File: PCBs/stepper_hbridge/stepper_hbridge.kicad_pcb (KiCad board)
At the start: 2 copper layers, 52.5 x 54.4 mm, 34 parts, among them J1 Conn_02x07_Odd_Even, J2 Conn_02x08_Odd_Even, J3 Conn_02x08_Odd_Even, J4 Conn_01x04_Pin, J5 Conn_01x04_Pin, J6 Conn_01x02_Pin, U1 L298N, U2 L298N, U3 NCP718xSN500

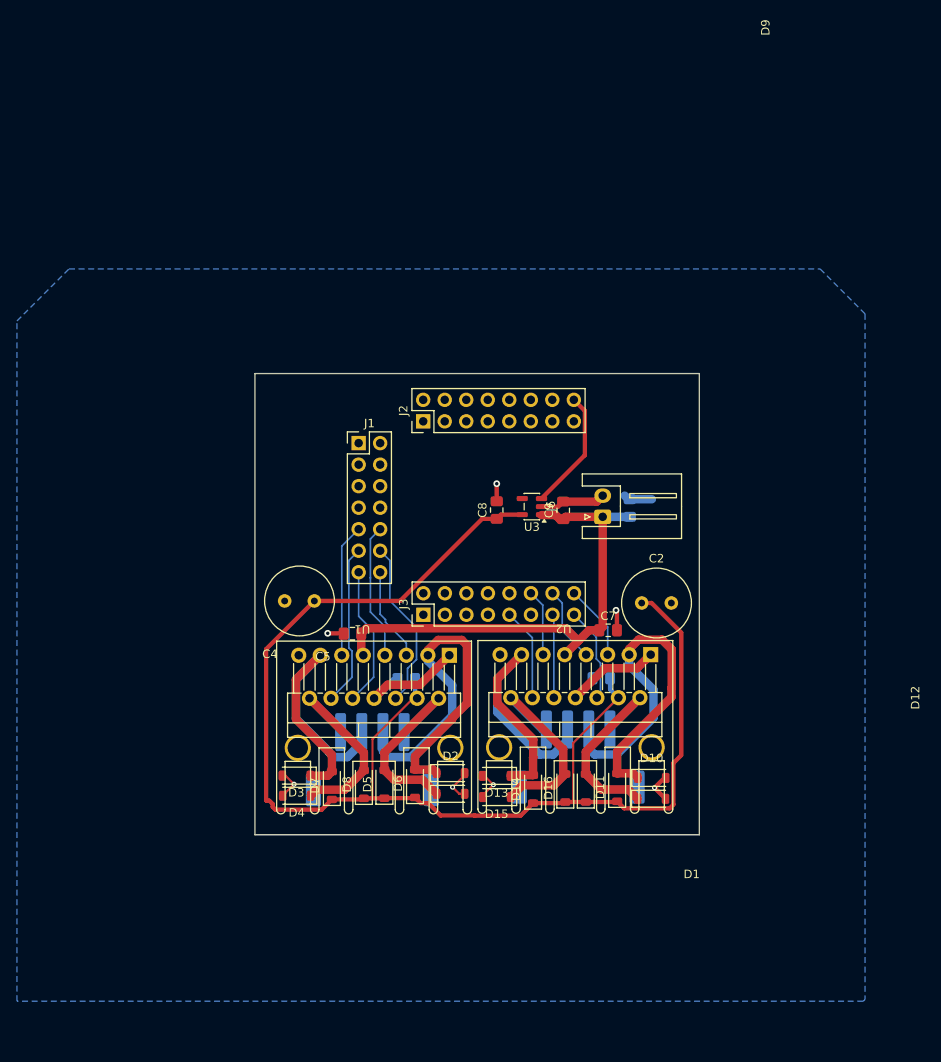
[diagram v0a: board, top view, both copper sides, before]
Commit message: fixed errors, need to add quadrature
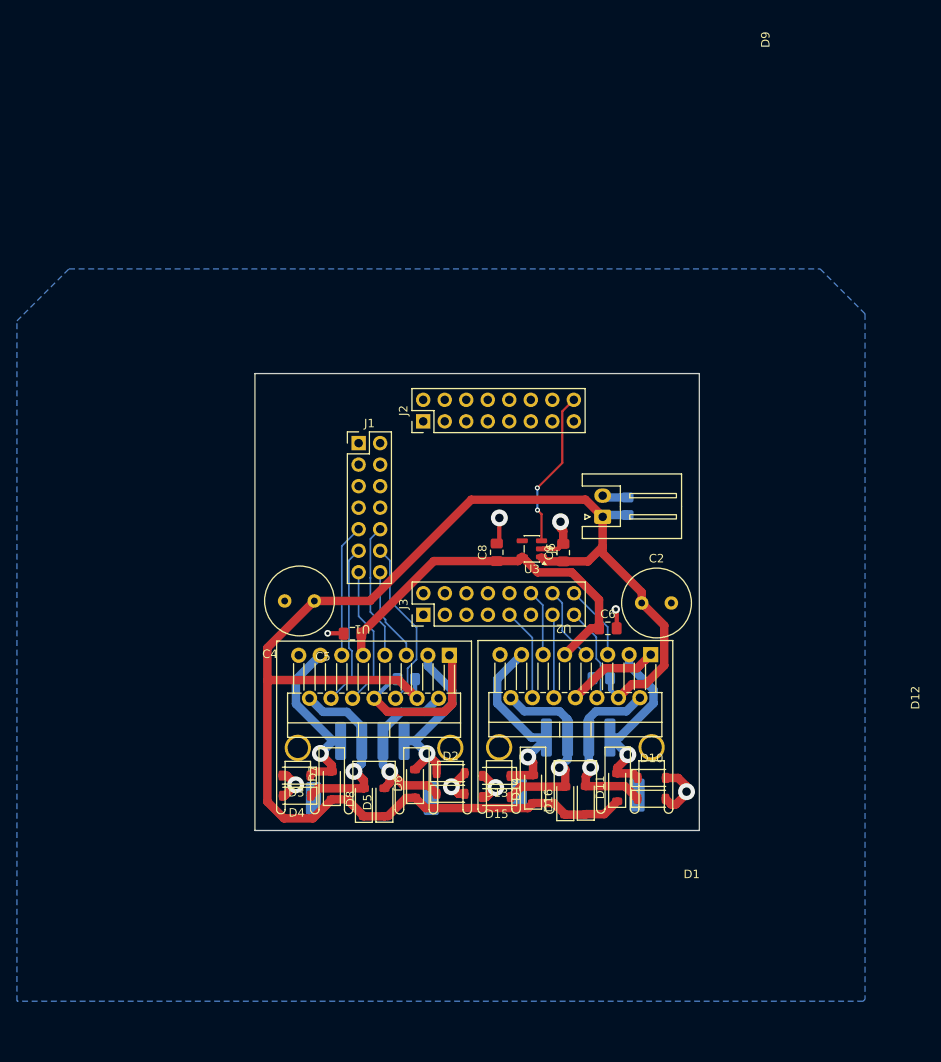
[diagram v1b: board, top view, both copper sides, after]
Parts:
- C6: moved to F.Cu
- C7: moved to B.Cu
- moved C7 14.8 mm to (158.0, 66.7), turned to 90 degrees
- moved C6 14.4 mm to (155.7, 81.1), turned to 0 degrees
- moved C8 4.99 mm to (142.6, 72.1)
- moved C9 4.99 mm to (150.4, 72.2)
- moved U3 4.99 mm to (146.7, 71.7)
- moved D5 2.12 mm to (129.3, 101.6)
- moved D8 2.12 mm to (126.9, 101.6)
- moved D16 1.49 mm to (150.7, 101.4)
- moved D9 1.43 mm to (153.1, 101.4)
- moved J4 1.04 mm to (127.9, 97.6)
- moved J5 0.95 mm to (152.2, 97.2)
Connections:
- C1 pad 1: +5V -> +24V
- C2 pad 1: +5V -> +24V
- C3 pad 1: +5V -> +24V
- C4 pad 1: +5V -> +24V
- C5 pad 1: +24V -> +5V
- C6 pad 1: +24V -> +5V
- D11 pad 1: +5V -> +24V
- D14 pad 1: +5V -> +24V
- D16 pad 1: +5V -> +24V
- D5 pad 1: +5V -> +24V
- D6 pad 1: +5V -> +24V
- D7 pad 1: +5V -> +24V
- D8 pad 1: +5V -> +24V
- D9 pad 1: +5V -> +24V
- J4 pad 1: Net-(D1-K) -> Net-(D2-K)
- J4 pad 2: Net-(D2-K) -> Net-(D1-K)
- J4 pad 3: Net-(D3-K) -> Net-(D4-K)
- J4 pad 4: Net-(D4-K) -> Net-(D3-K)
- J5 pad 1: Net-(D10-K) -> Net-(D11-A)
- J5 pad 2: Net-(D11-A) -> Net-(D10-K)
- J5 pad 3: Net-(D13-K) -> Net-(D15-K)
- J5 pad 4: Net-(D15-K) -> Net-(D13-K)
- U1 pad 4: +5V -> +24V
- U1 pad 9: +24V -> +5V
- U2 pad 4: +5V -> +24V
- U2 pad 9: +24V -> +5V
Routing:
- net +5V: track 166.8 -> 45.3 mm
- net +24V: track 58.7 -> 175.2 mm
- net Net-(D11-A): track 47.2 -> 22.1 mm, vias 0 -> 1
- net Net-(D2-K): track 47.4 -> 23.3 mm, vias 0 -> 1
- net Net-(D13-K): track 40.2 -> 22.7 mm, vias 0 -> 1
- net Net-(D3-K): track 39.7 -> 22.4 mm, vias 0 -> 1
- net GND: track 61.4 -> 69.3 mm, vias 7 -> 8
- net +3.3V: track 14.3 -> 18.6 mm, vias 0 -> 2
- net Net-(D10-K): track 24.2 -> 22.1 mm, vias 0 -> 1
- net Net-(D1-K): track 24.2 -> 22.2 mm, vias 0 -> 1
- net Net-(D4-K): track 24.2 -> 22.4 mm, vias 0 -> 1
- net Net-(D15-K): track 25.1 -> 23.7 mm, vias 0 -> 1
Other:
- board size 52.5 x 54.4 mm -> 52.5 x 53.9 mm

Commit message: stepper - changed diode placement, changed JSTXH to GH, changed main 24V connector
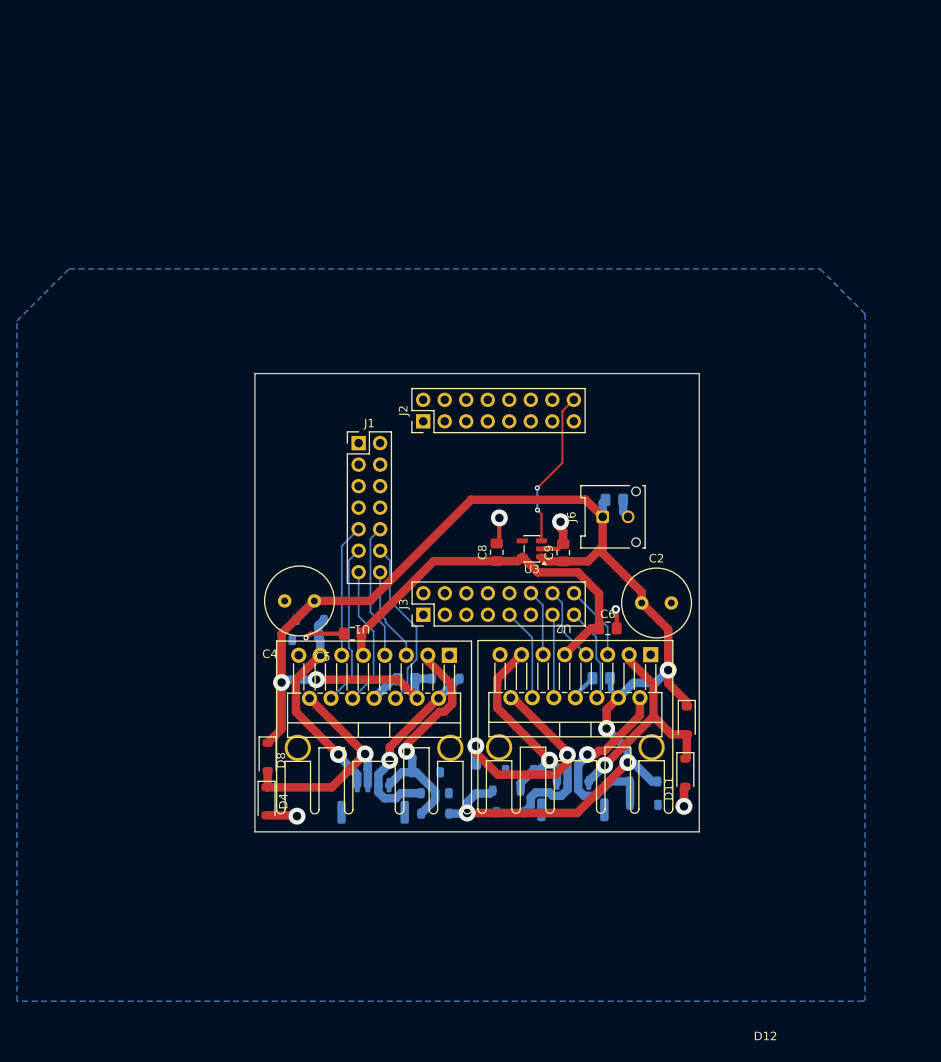
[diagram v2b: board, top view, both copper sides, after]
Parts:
- D1, D10, D13, D14, D15, D16, D2, D3, D5, D6, D7, D9: moved to B.Cu
- J4, J5: footprint Connector_JST:JST_XH_S4B-XH-SM4-TB_1x04-1MP_P2.50mm_Horizontal -> Connector_JST:JST_GH_SM04B-GHS-TB_1x04-1MP_P1.25mm_Horizontal
- J6: footprint Connector_JST:JST_XH_S2B-XH-A_1x02_P2.50mm_Horizontal -> Connector_Molex:Molex_Micro-Fit_3.0_43045-0212_2x01_P3.00mm_Vertical
- moved D7 19.7 mm to (120.5, 80.1), turned to 0 degrees
- moved D5 16.3 mm to (136.5, 87.0), turned to 0 degrees
- moved D3 16.0 mm to (120.1, 82.5)
- moved D8 12.6 mm to (115.5, 96.3), turned to -90 degrees
- moved D11 11.4 mm to (165.0, 92.0), turned to -90 degrees
- moved D16 10.8 mm to (140.1, 99.0)
- moved D9 7.16 mm to (159.9, 99.2), turned to 180 degrees
- moved D6 4.27 mm to (135.3, 103.0), turned to 180 degrees
- moved D12 4.01 mm to (164.8, 98.1), turned to -90 degrees
- moved J5 3.98 mm to (151.5, 101.2)
- moved J4 3.82 mm to (128.0, 101.5)
- moved D4 3.62 mm to (115.4, 101.5), turned to -90 degrees
- moved D14 3.12 mm to (143.7, 100.2), turned to 0 degrees
- moved D2 2.88 mm to (134.2, 98.1)
- moved D13 2.83 mm to (145.3, 97.8)
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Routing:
- net GND: track 69.3 -> 30.9 mm, vias 8 -> 6
- net Net-(D15-K): track 23.7 -> 37.4 mm, vias 1 -> 2
- net Net-(D4-K): track 22.4 -> 28.4 mm
- net Net-(D2-K): track 23.3 -> 28.6 mm
- net Net-(D11-A): track 22.1 -> 27.2 mm
- net Net-(D10-K): track 22.1 -> 24.7 mm
- net +24V: track 175.2 -> 172.9 mm, vias 0 -> 6
- net Net-(D13-K): track 22.7 -> 24.6 mm
- net Net-(D3-K): track 22.4 -> 24.0 mm
- net Net-(D1-K): track 22.2 -> 23.0 mm
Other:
- board size 52.5 x 53.9 mm -> 52.5 x 54.1 mm
